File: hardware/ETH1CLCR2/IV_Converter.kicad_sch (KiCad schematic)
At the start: 96 parts, among them K601 TQ2SA-5V, Q601 MMBFJ309LT1G, Q602 MMBFJ309LT1G, Q603 BC847, Q604 BC857, Q605 MMBFJ309LT1G, Q606 MMBFJ309LT1G, Q607 BC847, Q608 BC857, Q609 MMBFJ309LT1G, Q610 MMBFJ309LT1G, Q611 BC847, Q612 BC857, Q613 MMBFJ309LT1G, Q614 MMBFJ309LT1G, Q615 BC847, Q616 BC857, Q617 BC847, U601 SN74LVC1T45DBV, U602 SN74LVC1T45DBV, U603 SN74LVC1T45DBV, U604 SN74LVC1T45DBV, U605 ADA4817-1ARDZ

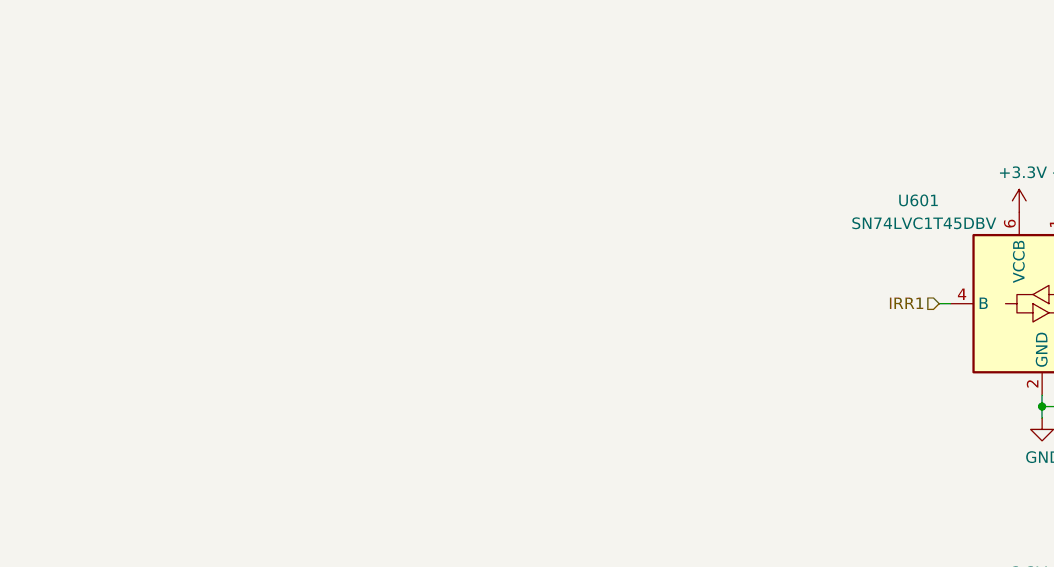
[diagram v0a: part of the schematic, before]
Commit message: Software development and added comments to the schematics.
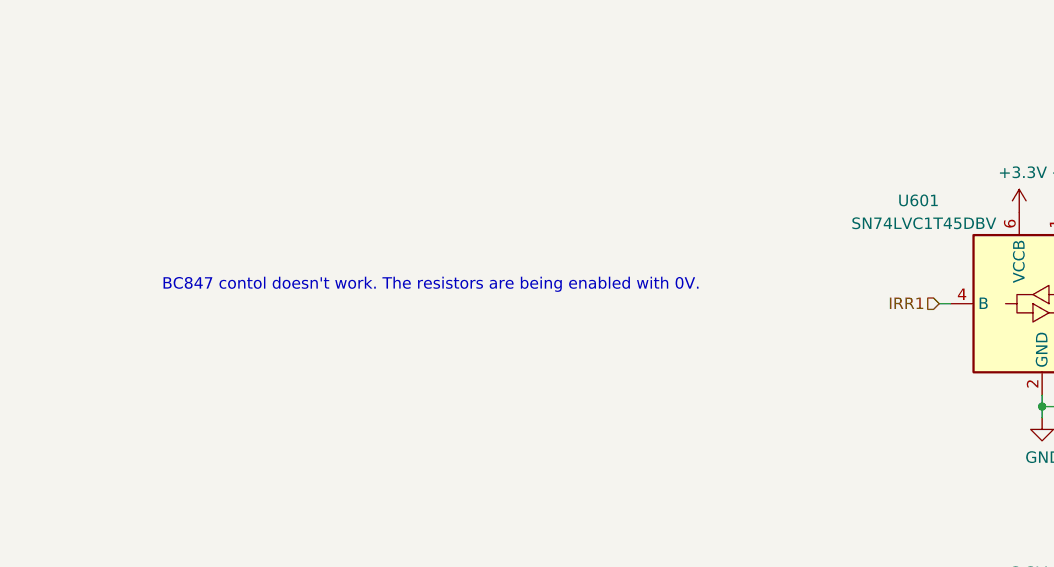
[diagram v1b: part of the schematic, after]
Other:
- note added: "BC847 contol doesn't work. The resistors are being enabled with 0V."
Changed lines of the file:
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@@
     (stroke (width 0) (type default) (color 0 0 0 0))
+  )
+  (text "BC847 contol doesn't work. The resistors are being enabled with 0V."
+    (at 31.75 50.8 0)
+    (effects (font (size 1.27 1.27)) (justify left bottom))
   )
   (hierarchical_label "L_CUR" (shape input) (at 114.3 217.17 180)

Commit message: Project updated
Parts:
- added R222, R223, R224, R225: 22k, Resistor_SMD:R_0603_1608Metric_Pad0.98x0.95mm_HandSolder, symbol Device:R
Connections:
- net -5VA: now also R222.2, R223.2, R224.2, R225.2
- net at Q603.1 (B), R605.1: now also R225.1
- net at Q607.1 (B), R612.1: now also R224.1
- net at Q611.1 (B), R619.1: now also R223.1
- net at Q615.1 (B), R626.1: now also R222.1
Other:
- moved on the sheet: R605, R612, R619, R626, U601, U602, U603, U604
